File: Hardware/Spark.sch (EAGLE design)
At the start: 8 parts

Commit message: begin v2
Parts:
- removed JP2, JP3: (no value), pinhead:PINHD-1X4
- removed U$1: TEENSY_3.1_BASIC, Teensy_3_Series_Board_v1.0:TEENSY_3.1_BASIC
- added C1, C2, C3, C4, C5: 0.1uF, SparkFun-Capacitors:0.1UF-25V-5%(0603)
- added C6, C7: 10uF, SparkFun-Capacitors:10UF50V20%(1210)
- added L1: 3.3uH, SparkFun-Passives:INDUCTOR0805
- added Q2: MMBT4403, SparkFun-DiscreteSemi:TRANSISTOR_PNPMMBT4403
- added R2: 8.2K, SparkFun-Resistors:8.2KOHM-1/10W-5%(0603)
- added R3, R4: 100, SparkFun-Resistors:100OHM-1/10W-1%(0603)
- added R5: 20k, SparkFun-Resistors:20KOHM1/10W1%(0603)
- added U1: HX711, Testing:HX711HX711
- JP4: device pinhead:PINHD-1X3 -> SparkFun-Connectors:M05PTH
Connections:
- removed net 3.3V: JP2.3, JP3.1, JP4.1, U$1.3.3V
- removed net CLK: JP3.3, U$1.3/CAN-TX/PWM
- removed net RX: JP2.2, U$1.0/RX1/T
- removed net TX: JP2.1, U$1.1/TX1/T
- removed net TX2: JP4.3, U$1.10/TX2/PWM
- new net A+: JP4.2, R4.1
- new net A-: JP4.3, R3.1
- new net AVDD: C3.1, C7.1, JP4.5, L1.1
- new net N$10: U1.DVDD
- new net N$3: C1.1, R3.2, U1.INA-
- new net N$4: Q2.B, U1.BASE
- new net N$5: L1.2, Q2.C, R5.2, U1.AVDD
- new net N$6: R2.2, R5.1, U1.VFB
- new net N$7: C2.2, U1.VBG
- new net N$8: C1.2, R4.2, U1.INA+
- new net SCK: U1.PD_SCK
- new net VDD: C4.1
- net DAT: now also U1.DOUT; no longer JP3.2, U$1.2
- net GND: now also C2.1, C3.2, C4.2, C5.2, C6.2, C7.2, JP4.1, JP4.4, R2.1, U1.AGND, U1.RATE, U1.XI; no longer JP2.4, JP3.4, JP4.2, U$1.GND
- net IGNITE: no longer U$1.4/CAN-RX-PWM
- net VCC: now also C5.1, C6.1, Q2.E, U1.VSUP
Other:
- note added: "A+"
- note added: "A-"
- note added: "AVDD = VBG(R1+R2)/R1"
- note added: "Black"
- note added: "Common Load Cell Colors:"
- note added: "E+"
- note added: "E-"
- note added: "Green or Blue"
- note added: "Red"
- note added: "Shield"
- note added: "VBG = 1.25V"
- note added: "White"
- note added: "Yellow"
- moved on the sheet: JP5

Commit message: 7-segment and arduino
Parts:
- added J1: ARDUINO_R3_SHIELD, SparkFun-Boards:ARDUINO_R3_SHIELD
- added R10, R11, R12, R13, R6, R7, R8, R9: 100, SparkFun:RESISTOR0402-RES
- added U$1: 7-SEGMENT-4DIGIT-COUNTERPTH, SparkFun-Displays:7-SEGMENT-4DIGIT-COUNTERPTH
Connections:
- removed net DAT: U1.DOUT
- new net A: J1.*D5, R6.2
- new net B: J1.*D6, R7.2
- new net C: J1.D7, R8.2
- new net D: J1.D8, R9.2
- new net DATA: J1.*D3, U1.DOUT
- new net DIG1: J1.D13, U$1.D1
- new net DIG2: J1.A0, U$1.D2
- new net DIG3: J1.A1, U$1.D3
- new net DIG4: J1.A2, U$1.D4
- new net DP: J1.D12, R13.2
- new net E: J1.*D9, R10.2
- new net F: J1.*D10, R11.2
- new net G: J1.*D11, R12.2
- new net N$11: R6.1, U$1.A
- new net N$12: R7.1, U$1.B
- new net N$14: R8.1, U$1.C
- new net N$15: R9.1, U$1.D
- new net N$16: R10.1, U$1.E
- new net N$17: R11.1, U$1.F
- new net N$18: R12.1, U$1.G
- new net N$19: R13.1, U$1.DP
- new net VIN: J1.VIN, JP1.2, JP5.1
- net IGNITE: now also J1.D4
- net SCK: now also J1.D2
- net VCC: now also J1.5V; no longer JP1.2, JP5.1
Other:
- note added: "7-Segment Display"
- note added: "Arduino"
- note added: "Load Cell"
- note added: "Power"
- moved on the sheet: C1, C2, C3, C4, C5, C6, C7, JP1, JP4, JP5, L1, Q1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

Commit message: prettify v2 schematic
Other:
- note added: "2.0"
- note added: "Ignition"
- note added: "Spark Static Testing Array"
- moved on the sheet: JP1, JP5, Q1, R1
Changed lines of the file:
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@@
 <text x="144.78" y="170.18" size="3.81" layer="94" font="vector">Load Cell</text>
 <wire x1="0" y1="160.02" x2="83.82" y2="160.02" width="0.1524" layer="94"/>
-<text x="35.56" y="53.34" size="3.81" layer="94" font="vector">Power</text>
+<text x="33.02" y="53.34" size="3.81" layer="94" font="vector">Power</text>
 <wire x1="83.82" y1="160.02" x2="185.42" y2="160.02" width="0.1524" layer="94"/>
 <text x="48.26" y="78.74" size="3.81" layer="94" font="vector">7-Segment
@@
 <wire x1="83.82" y1="93.98" x2="185.42" y2="93.98" width="0.1524" layer="94"/>
 <wire x1="0" y1="71.12" x2="83.82" y2="71.12" width="0.1524" layer="94"/>
+<text x="149.86" y="60.96" size="3.81" layer="94" font="vector">Ignition</text>
+<text x="88.9" y="27.94" size="3.81" layer="94" font="vector">Spark Static Testing Array</text>
+<text x="175.26" y="7.62" size="3.302" layer="94" font="vector">2.0</text>
 </plain>
 <instances>
-<instance part="Q1" gate="G$1" x="17.78" y="15.24"/>
-<instance part="GND1" gate="1" x="20.32" y="5.08"/>
-<instance part="R1" gate="G$1" x="12.7" y="20.32" rot="R270"/>
-<instance part="GND2" gate="1" x="12.7" y="30.48" rot="R180"/>
-<instance part="JP1" gate="G$1" x="20.32" y="30.48" rot="R270"/>
-<instance part="JP5" gate="G$1" x="76.2" y="15.24" rot="R180"/>
-<instance part="GND7" gate="1" x="68.58" y="5.08"/>
+<instance part="Q1" gate="G$1" x="111.76" y="60.96"/>
+<instance part="GND1" gate="1" x="114.3" y="50.8"/>
+<instance part="R1" gate="G$1" x="106.68" y="66.04" rot="R270"/>
+<instance part="GND2" gate="1" x="106.68" y="76.2" rot="R180"/>
+<instance part="JP1" gate="G$1" x="114.3" y="76.2" rot="R270"/>
+<instance part="JP5" gate="G$1" x="45.72" y="33.02" rot="R180"/>
+<instance part="GND7" gate="1" x="38.1" y="22.86"/>
 <instance part="U1" gate="U1" x="149.86" y="205.74"/>
 <instance part="Q2" gate="G$1" x="116.84" y="231.14" rot="MR0"/>
@@
 </instance>
 <instance part="SUPPLY4" gate="G$1" x="99.06" y="116.84" rot="R180"/>
-<instance part="SUPPLY5" gate="G$1" x="27.94" y="20.32" rot="R270"/>
-<instance part="SUPPLY6" gate="G$1" x="66.04" y="15.24" rot="R90"/>
+<instance part="SUPPLY5" gate="G$1" x="121.92" y="66.04" rot="R270"/>
+<instance part="SUPPLY6" gate="G$1" x="35.56" y="33.02" rot="R90"/>
 <instance part="SUPPLY8" gate="G$1" x="99.06" y="124.46"/>
 </instances>
@@
 <segment>
 <pinref part="Q1" gate="G$1" pin="G"/>
-<wire x1="15.24" y1="12.7" x2="12.7" y2="12.7" width="0.1524" layer="91"/>
-<label x="10.16" y="12.7" size="1.016" layer="95" rot="R180" xref="yes"/>
+<wire x1="109.22" y1="58.42" x2="106.68" y2="58.42" width="0.1524" layer="91"/>
+<label x="104.14" y="58.42" size="1.016" layer="95" rot="R180" xref="yes"/>
 <pinref part="R1" gate="G$1" pin="2"/>
-<wire x1="12.7" y1="12.7" x2="10.16" y2="12.7" width="0.1524" layer="91"/>
-<wire x1="12.7" y1="12.7" x2="12.7" y2="15.24" width="0.1524" layer="91"/>
-<junction x="12.7" y="12.7"/>
+<wire x1="106.68" y1="58.42" x2="104.14" y2="58.42" width="0.1524" layer="91"/>
+<wire x1="106.68" y1="58.42" x2="106.68" y2="60.96" width="0.1524" layer="91"/>
+<junction x="106.68" y="58.42"/>
 </segment>
 <segment>
@@
 <pinref part="R1" gate="G$1" pin="1"/>
 <pinref part="GND2" gate="1" pin="GND"/>
-<wire x1="12.7" y1="25.4" x2="12.7" y2="27.94" width="0.1524" layer="91"/>
+<wire x1="106.68" y1="71.12" x2="106.68" y2="73.66" width="0.1524" layer="91"/>
 </segment>
 <segment>
 <pinref part="Q1" gate="G$1" pin="S"/>
 <pinref part="GND1" gate="1" pin="GND"/>
-<wire x1="20.32" y1="10.16" x2="20.32" y2="7.62" width="0.1524" layer="91"/>
+<wire x1="114.3" y1="55.88" x2="114.3" y2="53.34" width="0.1524" layer="91"/>
 </segment>
 <segment>
 <pinref part="JP5" gate="G$1" pin="2"/>
-<wire x1="68.58" y1="12.7" x2="68.58" y2="7.62" width="0.1524" layer="91"/>
+<wire x1="38.1" y1="30.48" x2="38.1" y2="25.4" width="0.1524" layer="91"/>
 <pinref part="GND7" gate="1" pin="GND"/>
 </segment>
@@
 <pinref part="JP1" gate="G$1" pin="1"/>
 <pinref part="Q1" gate="G$1" pin="D"/>
-<wire x1="20.32" y1="22.86" x2="20.32" y2="20.32" width="0.1524" layer="91"/>
+<wire x1="114.3" y1="68.58" x2="114.3" y2="66.04" width="0.1524" layer="91"/>
 </segment>
 </net>
@@
 <segment>
 <pinref part="JP1" gate="G$1" pin="2"/>
-<wire x1="22.86" y1="22.86" x2="22.86" y2="20.32" width="0.1524" layer="91"/>
-<wire x1="22.86" y1="20.32" x2="27.94" y2="20.32" width="0.1524" layer="91"/>
+<wire x1="116.84" y1="68.58" x2="116.84" y2="66.04" width="0.1524" layer="91"/>
+<wire x1="116.84" y1="66.04" x2="121.92" y2="66.04" width="0.1524" layer="91"/>
 <pinref part="SUPPLY5" gate="G$1" pin="VIN"/>
 </segment>
 <segment>
 <pinref part="JP5" gate="G$1" pin="1"/>
-<wire x1="68.58" y1="15.24" x2="66.04" y2="15.24" width="0.1524" layer="91"/>
+<wire x1="38.1" y1="33.02" x2="35.56" y2="33.02" width="0.1524" layer="91"/>
 <pinref part="SUPPLY6" gate="G$1" pin="VIN"/>
 </segment>

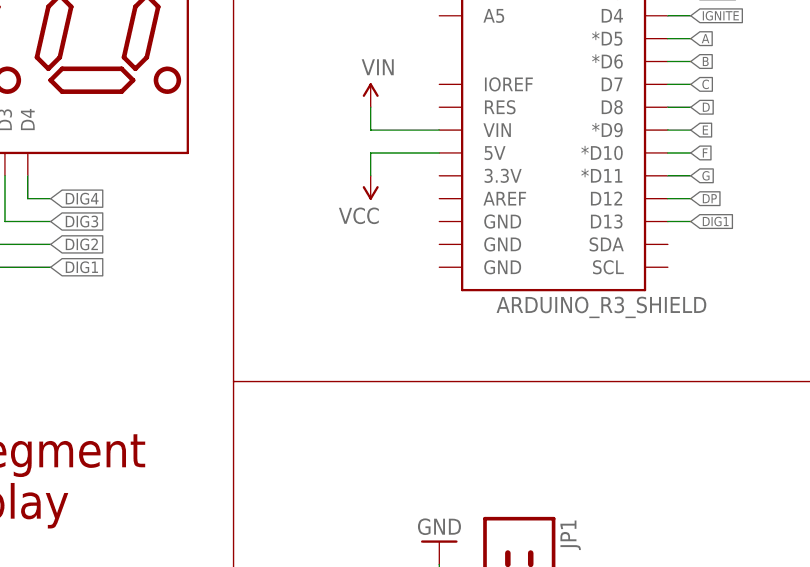
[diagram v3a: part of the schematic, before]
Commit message: ground arduino
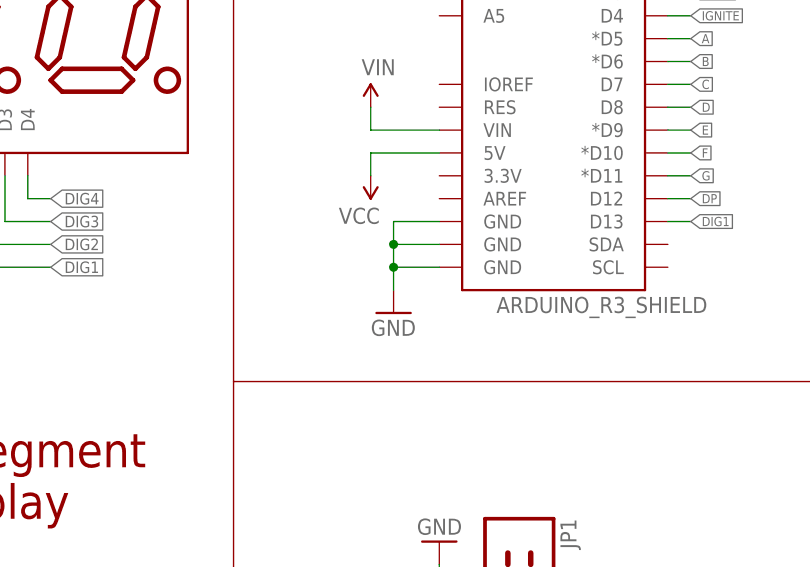
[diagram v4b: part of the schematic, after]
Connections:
- net GND: now also J1.GND@0, J1.GND@1, J1.GND@2
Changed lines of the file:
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@@
 <part name="SUPPLY6" library="SparkFun-Aesthetics" deviceset="VIN" device=""/>
 <part name="SUPPLY8" library="SparkFun-Aesthetics" deviceset="VIN" device=""/>
+<part name="GND3" library="SparkFun-Aesthetics" deviceset="GND" device=""/>
 </parts>
 <sheets>
@@
 <instance part="SUPPLY6" gate="G$1" x="35.56" y="33.02" rot="R90"/>
 <instance part="SUPPLY8" gate="G$1" x="99.06" y="124.46"/>
+<instance part="GND3" gate="1" x="101.6" y="101.6"/>
 </instances>
 <busses>
@@
 <pinref part="C4" gate="G$1" pin="2"/>
 </segment>
+<segment>
+<pinref part="J1" gate="G$1" pin="GND@2"/>
+<pinref part="GND3" gate="1" pin="GND"/>
+<wire x1="106.68" y1="111.76" x2="101.6" y2="111.76" width="0.1524" layer="91"/>
+<wire x1="101.6" y1="111.76" x2="101.6" y2="109.22" width="0.1524" layer="91"/>
+<pinref part="J1" gate="G$1" pin="GND@1"/>
+<wire x1="101.6" y1="109.22" x2="101.6" y2="106.68" width="0.1524" layer="91"/>
+<wire x1="101.6" y1="106.68" x2="101.6" y2="104.14" width="0.1524" layer="91"/>
+<wire x1="106.68" y1="109.22" x2="101.6" y2="109.22" width="0.1524" layer="91"/>
+<junction x="101.6" y="109.22"/>
+<pinref part="J1" gate="G$1" pin="GND@0"/>
+<wire x1="101.6" y1="106.68" x2="106.68" y2="106.68" width="0.1524" layer="91"/>
+<junction x="101.6" y="106.68"/>
+</segment>
 </net>

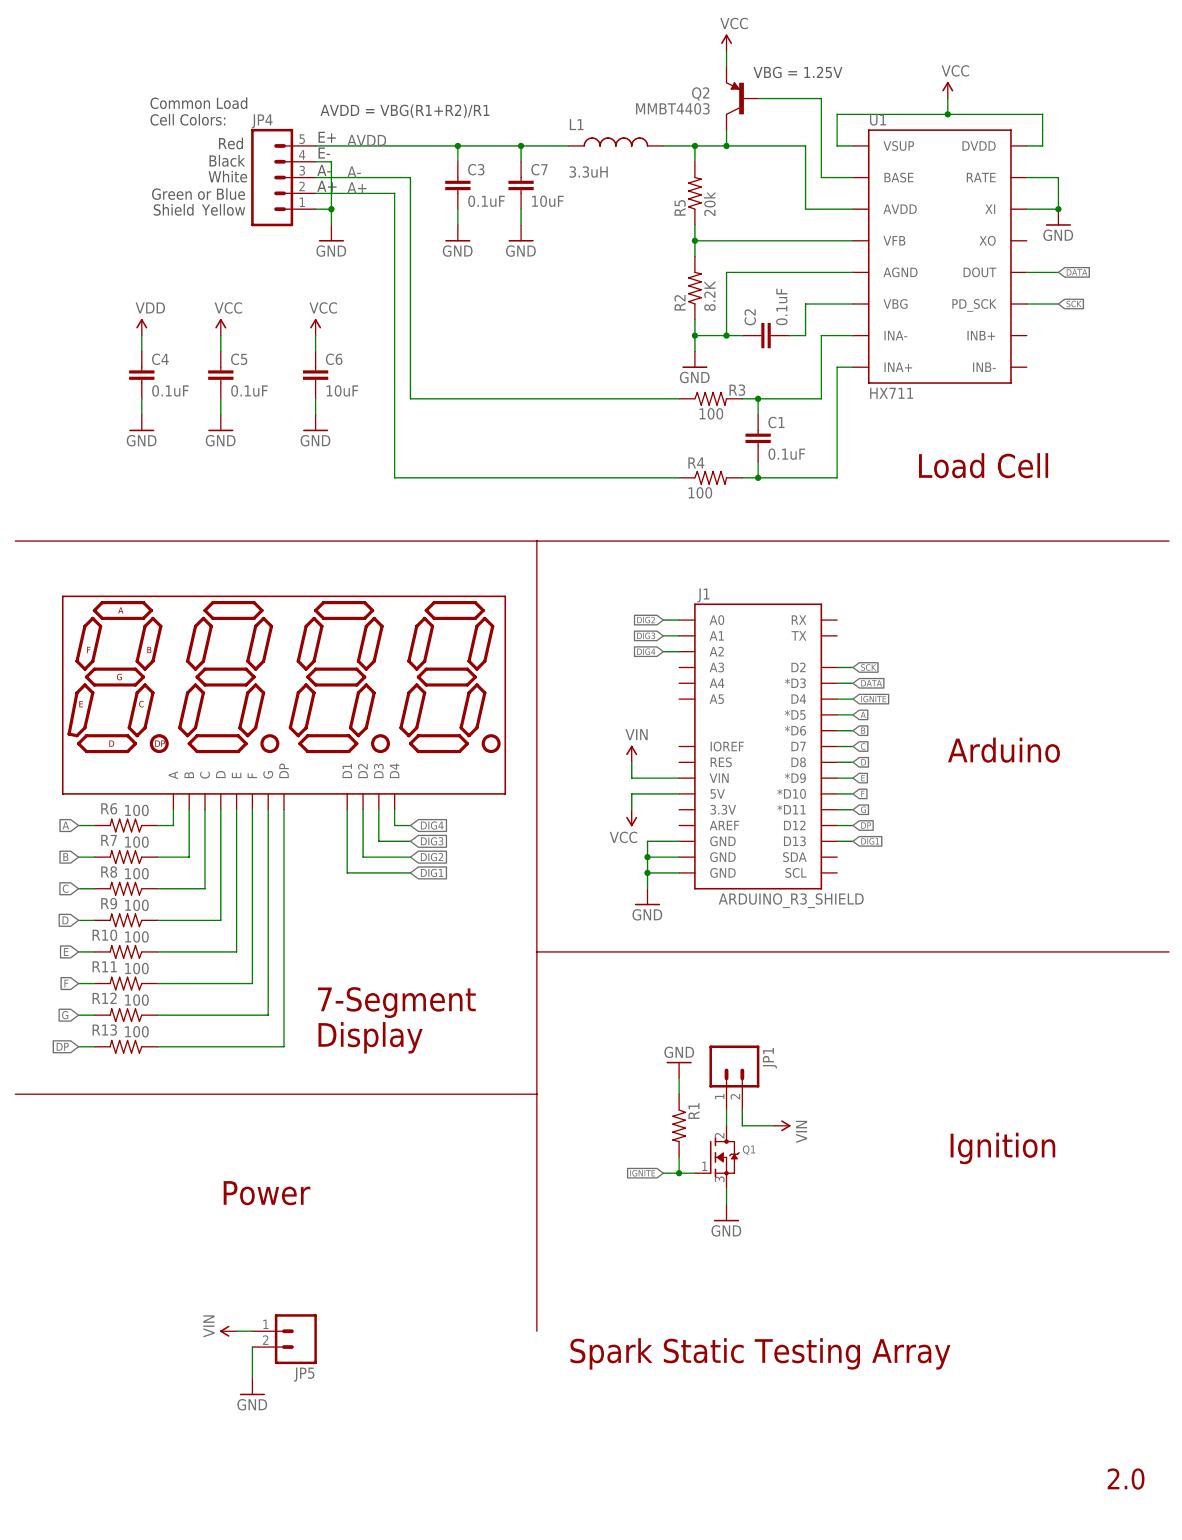
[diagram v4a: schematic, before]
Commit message: switch to 0805 packages
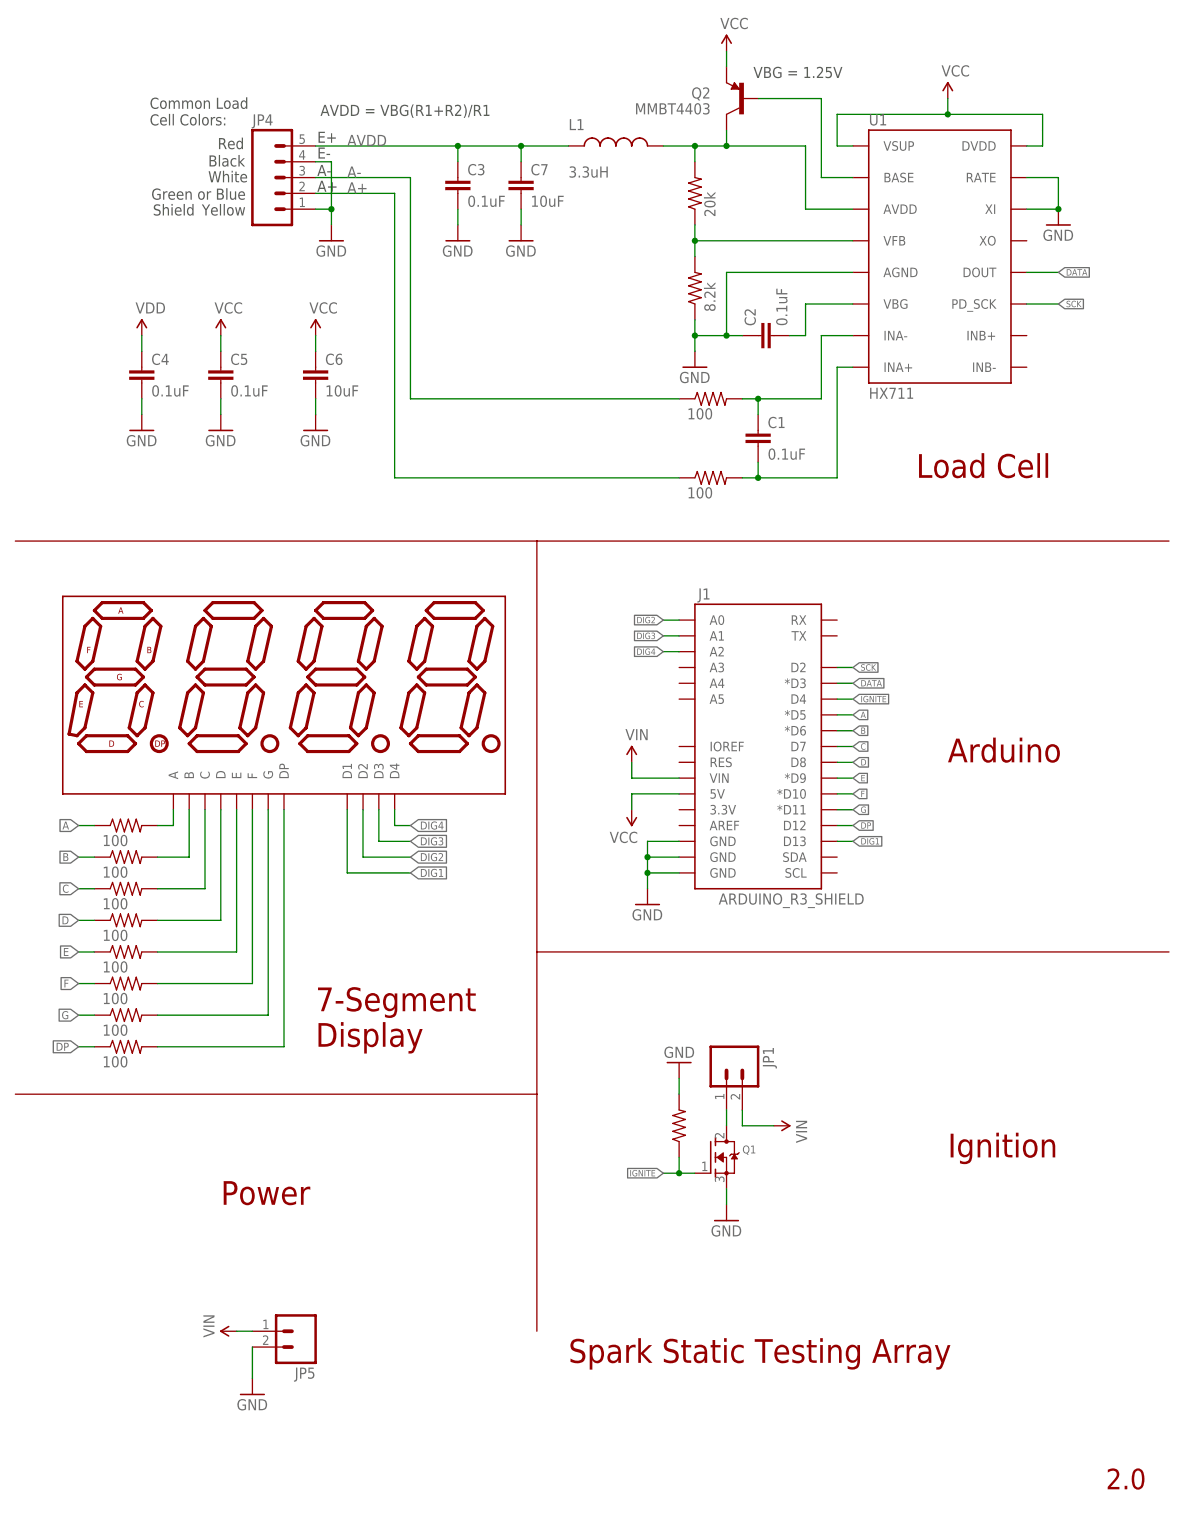
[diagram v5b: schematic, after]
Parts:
- removed R2: 8.2K, SparkFun-Resistors:8.2KOHM-1/10W-5%(0603)
- removed R5: 20k, SparkFun-Resistors:20KOHM1/10W1%(0603)
- added R14: 8.2k, SparkFun-Resistors:RESISTOR0805-RES
- added R15: 20k, SparkFun-Resistors:RESISTOR0805-RES
- R1: device SparkFun-Passives:RESISTOREZ -> SparkFun-Resistors:RESISTOR0805-RES
- R10, R11, R12, R13, R6, R7, R8, R9: device SparkFun:RESISTOR0402-RES -> SparkFun-Resistors:RESISTOR0805-RES
- R3, R4: device SparkFun-Resistors:100OHM-1/10W-1%(0603) -> SparkFun-Resistors:RESISTOR0805-RES
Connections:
- net A: now also R13.1; no longer R6.2
- net B: now also R6.1; no longer R7.2
- net C: now also R7.1; no longer R8.2
- net D: now also R8.1; no longer R9.2
- net DP: now also R12.1; no longer R13.2
- net E: now also R9.1; no longer R10.2
- net F: now also R10.1; no longer R11.2
- net G: now also R11.1; no longer R12.2
- net GND: now also R1.2, R14.1; no longer R1.1, R2.1
- net IGNITE: now also R1.1; no longer R1.2
- net N$11: now also R13.2; no longer R6.1
- net N$12: now also R6.2; no longer R7.1
- net N$14: now also R7.2; no longer R8.1
- net N$15: now also R8.2; no longer R9.1
- net N$16: now also R9.2; no longer R10.1
- net N$17: now also R10.2; no longer R11.1
- net N$18: now also R11.2; no longer R12.1
- net N$19: now also R12.2; no longer R13.1
- net N$5: now also R15.2; no longer R5.2
- net N$6: now also R14.2, R15.1; no longer R2.2, R5.1
